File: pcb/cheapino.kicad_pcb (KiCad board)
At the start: 2 copper layers, 132.5 x 95.1 mm, 59 parts, among them K1 SW_Push, K10 SW_Push, K11 SW_Push, K12 SW_Push, K13 SW_Push, K14 SW_Push, K15 SW_Push, K16 SW_Push, K17 SW_Push, K18 SW_Push, K2 SW_Push, K3 SW_Push, K4 SW_Push, K5 SW_Push, K6 SW_Push, K7 SW_Push, K8 SW_Push, K9 SW_Push, U1 RP2040-Zero

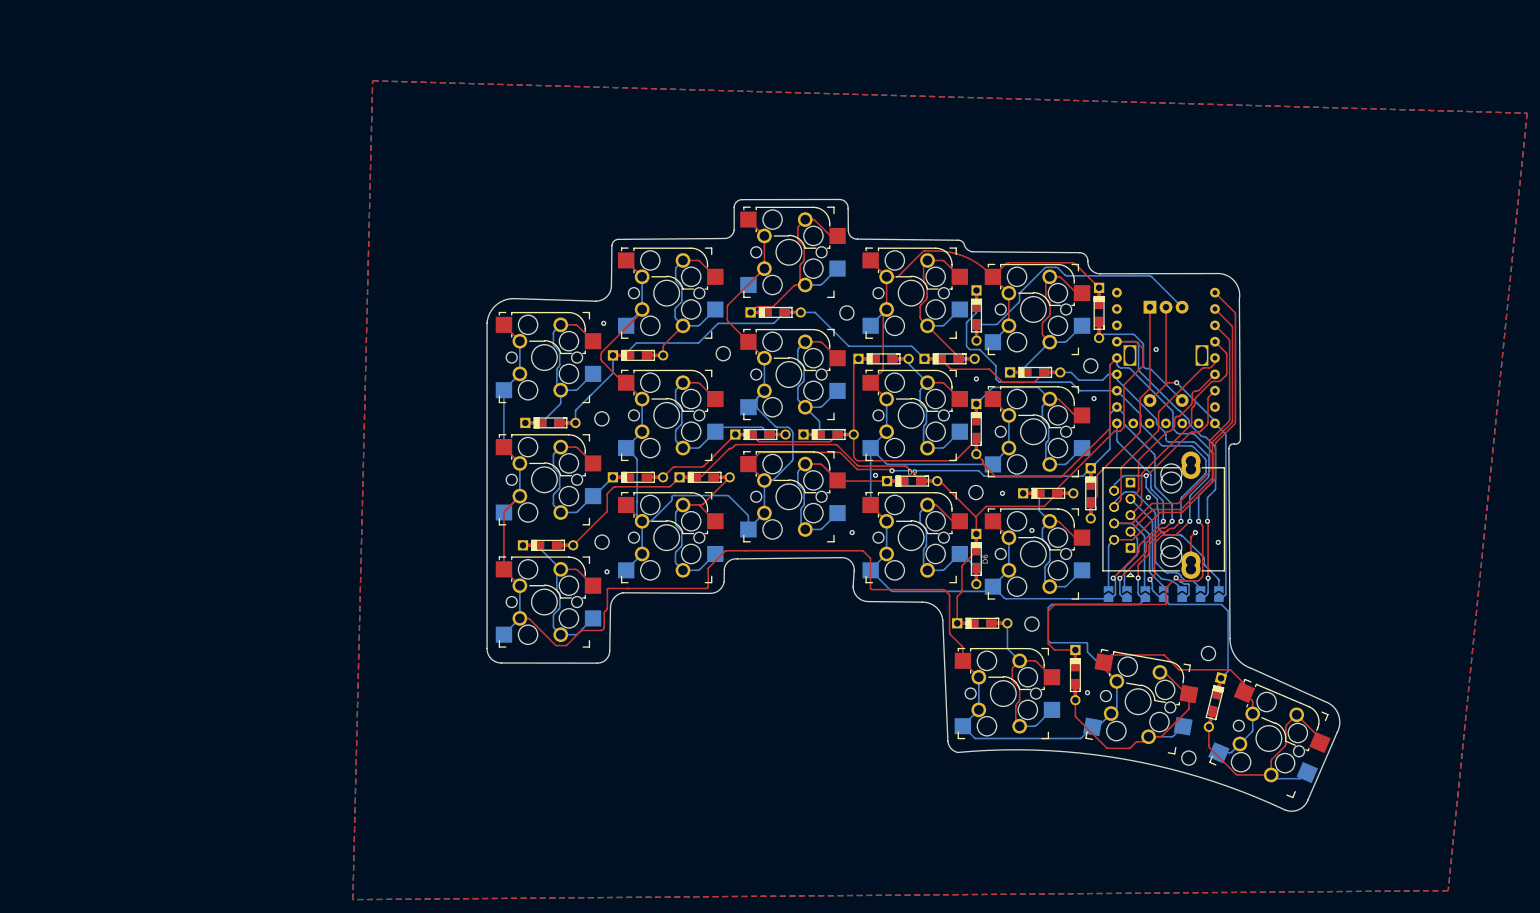
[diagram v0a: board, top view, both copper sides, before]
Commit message: Removed Rotary Encoder for space/flippability reasons and replaced all the key switch footprints that weren't bound properly to the schematic for some reason.
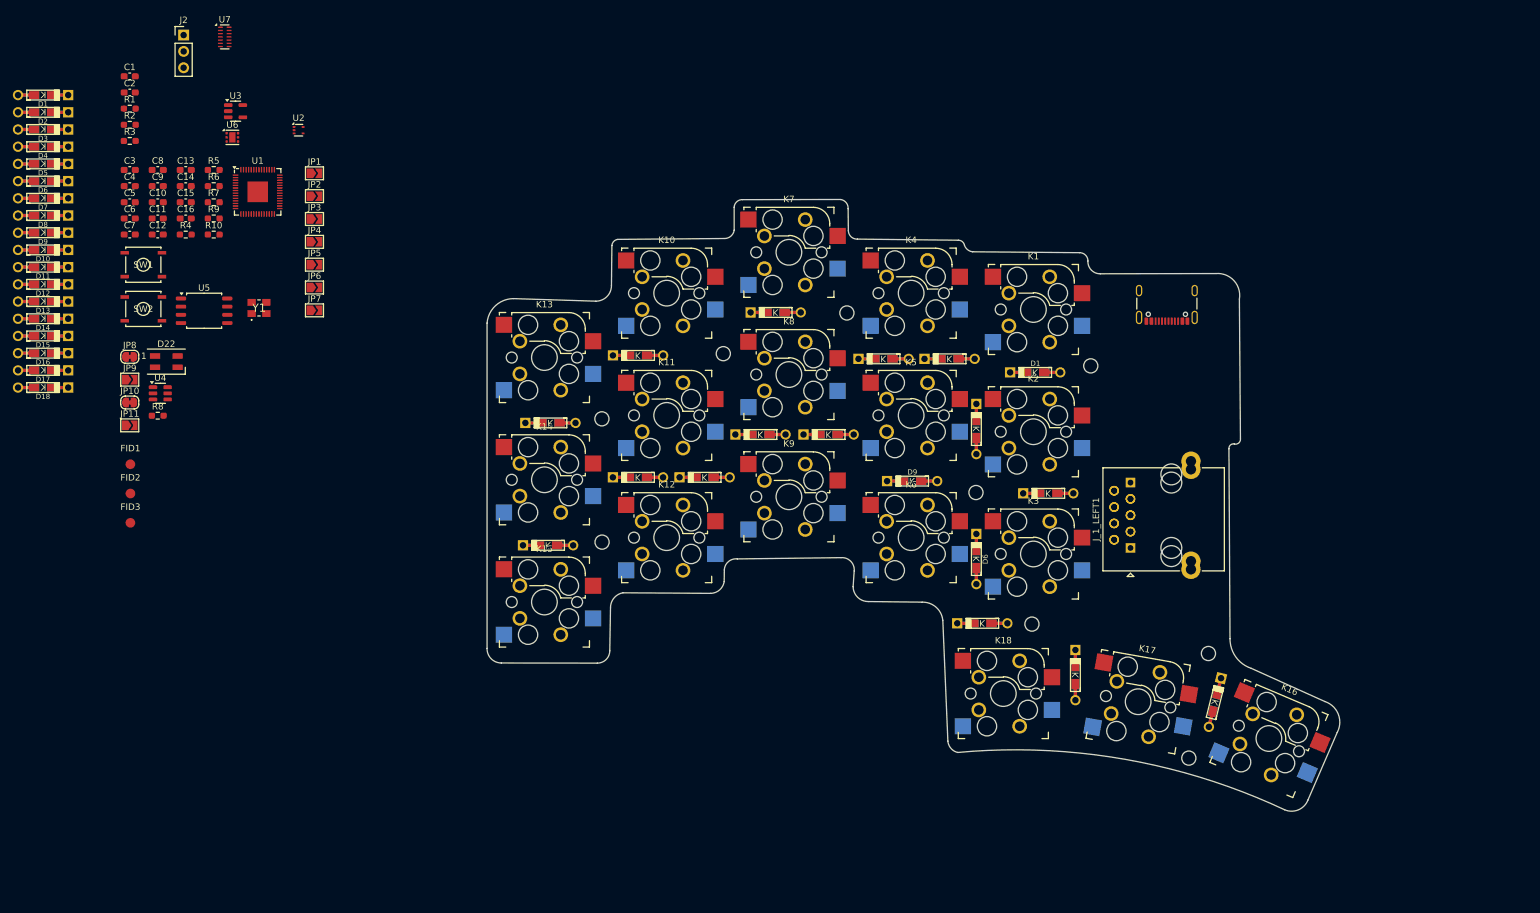
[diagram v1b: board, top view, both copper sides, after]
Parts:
- removed D19, D20, D21: DIODE, keebio:Diode-dual
- removed ENC1: RotaryEncoder_Switch, Rotary_Encoder:RotaryEncoder_Alps_EC11E-Switch_Vertical_H20mm
- added C1: 1μF, Capacitor_SMD:C_0603_1608Metric_Pad1.08x0.95mm_HandSolder, F.Cu at (4.57, 26.6)
- added C10: 1μF, Capacitor_SMD:C_0603_1608Metric_Pad1.08x0.95mm_HandSolder, F.Cu at (8.91, 46.2)
- added C11: 1μF, Capacitor_SMD:C_0603_1608Metric_Pad1.08x0.95mm_HandSolder, F.Cu at (8.91, 48.7)
- added C12: 100nF, Capacitor_SMD:C_0603_1608Metric_Pad1.08x0.95mm_HandSolder, F.Cu at (8.91, 51.2)
- added C13: 100nF, Capacitor_SMD:C_0603_1608Metric_Pad1.08x0.95mm_HandSolder, F.Cu at (13.3, 41.2)
- added C14: 15pF, Capacitor_SMD:C_0603_1608Metric_Pad1.08x0.95mm_HandSolder, F.Cu at (13.3, 43.7)
- added C15: 15pF, Capacitor_SMD:C_0603_1608Metric_Pad1.08x0.95mm_HandSolder, F.Cu at (13.3, 46.2)
- added C16: 100nF, Capacitor_SMD:C_0603_1608Metric_Pad1.08x0.95mm_HandSolder, F.Cu at (13.3, 48.7)
- added C2: 1μF, Capacitor_SMD:C_0603_1608Metric_Pad1.08x0.95mm_HandSolder, F.Cu at (4.57, 29.1)
- added C3: 100nF, Capacitor_SMD:C_0603_1608Metric_Pad1.08x0.95mm_HandSolder, F.Cu at (4.57, 41.2)
- added C4: 100nF, Capacitor_SMD:C_0603_1608Metric_Pad1.08x0.95mm_HandSolder, F.Cu at (4.57, 43.7)
- added C5: 100nF, Capacitor_SMD:C_0603_1608Metric_Pad1.08x0.95mm_HandSolder, F.Cu at (4.57, 46.2)
- added C6: 100nF, Capacitor_SMD:C_0603_1608Metric_Pad1.08x0.95mm_HandSolder, F.Cu at (4.57, 48.7)
- added C7: 100nF, Capacitor_SMD:C_0603_1608Metric_Pad1.08x0.95mm_HandSolder, F.Cu at (4.57, 51.2)
- added C8: 100nF, Capacitor_SMD:C_0603_1608Metric_Pad1.08x0.95mm_HandSolder, F.Cu at (8.91, 41.2)
- added C9: 100nF, Capacitor_SMD:C_0603_1608Metric_Pad1.08x0.95mm_HandSolder, F.Cu at (8.91, 43.7)
- added D1: DIODE, keebio:Diode-dual, F.Cu at (-8.90, 29.5)
- added D10: DIODE, keebio:Diode-dual, F.Cu at (-8.90, 53.6)
- added D11: DIODE, keebio:Diode-dual, F.Cu at (-8.90, 56.3)
- added D12: DIODE, keebio:Diode-dual, F.Cu at (-8.90, 59.0)
- added D13: DIODE, keebio:Diode-dual, F.Cu at (-8.90, 61.6)
- added D14: DIODE, keebio:Diode-dual, F.Cu at (-8.90, 64.3)
- added D15: DIODE, keebio:Diode-dual, F.Cu at (-8.90, 67.0)
- added D16: DIODE, keebio:Diode-dual, F.Cu at (-8.90, 69.7)
- added D17: DIODE, keebio:Diode-dual, F.Cu at (-8.90, 72.3)
- added D18: DIODE, keebio:Diode-dual, F.Cu at (-8.90, 75.0)
- added D2: DIODE, keebio:Diode-dual, F.Cu at (-8.90, 32.2)
- added D22: SK6812MINI, LED_SMD:LED_SK6812MINI_PLCC4_3.5x3.5mm_P1.75mm, F.Cu at (10.2, 71.0)
- added D3: DIODE, keebio:Diode-dual, F.Cu at (-8.90, 34.9)
- added D4: DIODE, keebio:Diode-dual, F.Cu at (-8.90, 37.6)
- added D5: DIODE, keebio:Diode-dual, F.Cu at (-8.90, 40.2)
- added D6: DIODE, keebio:Diode-dual, F.Cu at (-8.90, 42.9)
- added D7: DIODE, keebio:Diode-dual, F.Cu at (-8.90, 45.6)
- added D8: DIODE, keebio:Diode-dual, F.Cu at (-8.90, 48.3)
- added D9: DIODE, keebio:Diode-dual, F.Cu at (-8.90, 50.9)
- added FID1: Fiducial, Fiducial:Fiducial_1.5mm_Mask3mm, F.Cu at (4.67, 86.9)
- added FID2: Fiducial, Fiducial:Fiducial_1.5mm_Mask3mm, F.Cu at (4.67, 91.5)
- added FID3: Fiducial, Fiducial:Fiducial_1.5mm_Mask3mm, F.Cu at (4.67, 96.0)
- added J1: USB_C_Receptacle_USB2.0_16P, Connector_USB:USB_C_Receptacle_GCT_USB4105-xx-A_16P_TopMnt_Horizontal, F.Cu at (165.8, 61.0)
- added J2: DBG, Connector_PinHeader_2.54mm:PinHeader_1x03_P2.54mm_Vertical, F.Cu at (12.9, 20.2)
- added JP10: LED_DriveAs3V3, Jumper:SolderJumper-2_P1.3mm_Bridged_RoundedPad1.0x1.5mm, F.Cu at (4.57, 77.3)
- added JP11: LED_DriveAs5V, Jumper:SolderJumper-2_P1.3mm_Open_TrianglePad1.0x1.5mm, F.Cu at (4.57, 80.9)
- added JP8: LED_DriveAs3V3, Jumper:SolderJumper-2_P1.3mm_Bridged_RoundedPad1.0x1.5mm, F.Cu at (4.57, 70.2)
- added JP9: LED_DriveAs5V, Jumper:SolderJumper-2_P1.3mm_Open_TrianglePad1.0x1.5mm, F.Cu at (4.57, 73.8)
- added R1: 5.1k, Resistor_SMD:R_0603_1608Metric_Pad0.98x0.95mm_HandSolder, F.Cu at (4.57, 31.6)
- added R10: 1k, Resistor_SMD:R_0603_1608Metric_Pad0.98x0.95mm_HandSolder, F.Cu at (17.6, 51.2)
- added R2: 5.1k, Resistor_SMD:R_0603_1608Metric_Pad0.98x0.95mm_HandSolder, F.Cu at (4.57, 34.2)
- added R3: 10k, Resistor_SMD:R_0603_1608Metric_Pad0.98x0.95mm_HandSolder, F.Cu at (4.57, 36.7)
- added R4: 10k, Resistor_SMD:R_0603_1608Metric_Pad0.98x0.95mm_HandSolder, F.Cu at (13.3, 51.2)
- added R5: 27, Resistor_SMD:R_0603_1608Metric_Pad0.98x0.95mm_HandSolder, F.Cu at (17.6, 41.2)
- added R6: 27, Resistor_SMD:R_0603_1608Metric_Pad0.98x0.95mm_HandSolder, F.Cu at (17.6, 43.7)
- added R7: 1k, Resistor_SMD:R_0603_1608Metric_Pad0.98x0.95mm_HandSolder, F.Cu at (17.6, 46.2)
- added R8: 470, Resistor_SMD:R_0603_1608Metric_Pad0.98x0.95mm_HandSolder, F.Cu at (8.91, 79.4)
- added R9: 10k, Resistor_SMD:R_0603_1608Metric_Pad0.98x0.95mm_HandSolder, F.Cu at (17.6, 48.7)
- added SW1: BOOT, Extra:TL3342_EWI, F.Cu at (6.67, 55.9)
- added SW2: RST, Extra:TL3342_EWI, F.Cu at (6.67, 62.8)
- added U2: TPD2E2U06, Package_TO_SOT_SMD:SOT-553, F.Cu at (30.8, 35.0)
- added U3: AP2112K-3.3, Package_TO_SOT_SMD:SOT-23-5, F.Cu at (21.0, 32.0)
- added U4: TXS0101DBV, Package_TO_SOT_SMD:SOT-23-6, F.Cu at (9.31, 75.9)
- added U5: W25Q128JVSIQ, Package_SO:SOIC-8_5.23x5.23mm_P1.27mm, F.Cu at (16.1, 63.1)
- added U6: TVS0500DRV, Package_SON:WSON-6-1EP_2x2mm_P0.65mm_EP1x1.6mm, F.Cu at (20.5, 36.1)
- added U7: TPD6E05U06RVZ, Package_SON:Texas_R-PUSON-N14, F.Cu at (19.3, 20.5)
- added Y1: 12MHz, Extra:ABM8272T3, F.Cu at (24.6, 62.6)
- JP1, JP2, JP3, JP4, JP5, JP6, JP7: moved to F.Cu
- K1, K10, K11, K12, K13, K14, K15, K16, K17, K18, K2, K3, K4, K5, K6, K7, K8, K9: footprint project_footprints:Kailh_socket_MX_optional_reversible -> keyswitches:Kailh_socket_MX_optional_reversible
- U1: value RP2040-Zero -> RP2040; footprint rp2040:MCU_RP2040_Zero_34 -> Package_DFN_QFN:QFN-56-1EP_7x7mm_P0.4mm_EP3.2x3.2mm
- moved JP7 147.3 mm to (33.3, 63.0), turned to 0 degrees
- moved JP6 145.7 mm to (33.3, 59.5), turned to 0 degrees
- moved JP5 144.2 mm to (33.3, 55.9), turned to 0 degrees
- moved JP4 142.9 mm to (33.3, 52.4), turned to 0 degrees
- moved JP3 141.7 mm to (33.3, 48.8), turned to 0 degrees
- moved JP2 140.6 mm to (33.3, 45.2), turned to 0 degrees
- moved U1 140.6 mm to (24.4, 44.6)
- moved JP1 139.7 mm to (33.3, 41.7), turned to 0 degrees
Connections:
- JP1 pad 1: COL_1 -> /KeySwitches/COL_1
- JP1 pad 2: R_COL_1 -> /ExtConnectors/C_R_COL_1
- JP2 pad 1: COL_2 -> /KeySwitches/COL_2
- JP2 pad 2: R_COL_2 -> /ExtConnectors/C_R_COL_2
- JP3 pad 1: COL_3 -> /KeySwitches/COL_3
- JP3 pad 2: R_COL_3 -> /ExtConnectors/C_R_COL_3
- JP4 pad 1: ROW_1 -> /KeySwitches/ROW_1
- JP4 pad 2: R_ROW_1 -> /ExtConnectors/C_R_ROW_1
- JP5 pad 1: ROW_2 -> /KeySwitches/ROW_2
- JP5 pad 2: R_ROW_3 -> /ExtConnectors/C_R_ROW_3
- JP6 pad 1: ROW_3 -> /KeySwitches/ROW_3
- JP6 pad 2: R_ROW_2 -> /ExtConnectors/C_R_ROW_2
- JP7 pad 1: ROW_4 -> /LeftRightMapping/ROW_4
- JP7 pad 2: R_ROW_4 -> /LeftRightMapping/R_ROW_4
- J_1_LEFT1 pad 2: R_COL_1 -> /ExtConnectors/C_R_COL_1
- J_1_LEFT1 pad 3: R_COL_2 -> /ExtConnectors/C_R_COL_2
- J_1_LEFT1 pad 4: R_COL_3 -> /ExtConnectors/C_R_COL_3
- J_1_LEFT1 pad 5: R_ROW_1 -> /ExtConnectors/C_R_ROW_1
- J_1_LEFT1 pad 6: R_ROW_2 -> /ExtConnectors/C_R_ROW_2
- J_1_LEFT1 pad 7: R_ROW_3 -> /ExtConnectors/C_R_ROW_3
- J_1_LEFT1 pad 8: R_ROW_4 -> GND
- J_2_RIGHT1 pad 2: R_ROW_4 -> GND
- J_2_RIGHT1 pad 3: R_ROW_3 -> /ExtConnectors/C_R_ROW_3
- J_2_RIGHT1 pad 4: R_ROW_2 -> /ExtConnectors/C_R_ROW_2
- J_2_RIGHT1 pad 5: R_ROW_1 -> /ExtConnectors/C_R_ROW_1
- J_2_RIGHT1 pad 6: R_COL_3 -> /ExtConnectors/C_R_COL_3
- J_2_RIGHT1 pad 7: R_COL_2 -> /ExtConnectors/C_R_COL_2
- J_2_RIGHT1 pad 8: R_COL_1 -> /ExtConnectors/C_R_COL_1
- K1 pad 1: COL_1 -> /KeySwitches/COL_3
- K1 pad 2: Net-(D1-K) -> Net-(D1-A)
- K10 pad 1: COL_2 -> /KeySwitches/COL_2
- K10 pad 2: Net-(D10-A) -> Net-(D10-K)
- K11 pad 1: COL_2 -> /KeySwitches/COL_2
- K11 pad 2: Net-(D11-A) -> Net-(D11-K)
- K12 pad 1: COL_2 -> /KeySwitches/COL_2
- K12 pad 2: Net-(D12-A) -> Net-(D12-K)
- K13 pad 1: COL_3 -> /KeySwitches/COL_1
- K13 pad 2: Net-(D13-K) -> Net-(D13-A)
- K14 pad 1: COL_3 -> /KeySwitches/COL_1
- K14 pad 2: Net-(D14-K) -> Net-(D14-A)
- K15 pad 1: COL_3 -> /KeySwitches/COL_1
- K15 pad 2: Net-(D15-K) -> Net-(D15-A)
- K16 pad 1: COL_3 -> /KeySwitches/COL_1
- K16 pad 2: Net-(D16-A) -> Net-(D16-K)
- K17 pad 1: COL_3 -> /KeySwitches/COL_1
- K17 pad 2: Net-(D17-A) -> Net-(D17-K)
- K18 pad 1: COL_3 -> /KeySwitches/COL_1
- K18 pad 2: Net-(D18-A) -> Net-(D18-K)
- K2 pad 1: COL_1 -> /KeySwitches/COL_3
- K2 pad 2: Net-(D2-K) -> Net-(D2-A)
- K3 pad 1: COL_1 -> /KeySwitches/COL_3
- K3 pad 2: Net-(D3-K) -> Net-(D3-A)
- K4 pad 1: COL_1 -> /KeySwitches/COL_3
- K4 pad 2: Net-(D4-A) -> Net-(D4-K)
- K5 pad 1: COL_1 -> /KeySwitches/COL_3
- K5 pad 2: Net-(D5-A) -> Net-(D5-K)
- K6 pad 1: COL_1 -> /KeySwitches/COL_3
- K6 pad 2: Net-(D6-A) -> Net-(D6-K)
- K7 pad 1: COL_2 -> /KeySwitches/COL_2
- K7 pad 2: Net-(D7-K) -> Net-(D7-A)
- K8 pad 1: COL_2 -> /KeySwitches/COL_2
- K8 pad 2: Net-(D8-K) -> Net-(D8-A)
- K9 pad 1: COL_2 -> /KeySwitches/COL_2
- K9 pad 2: Net-(D9-K) -> Net-(D9-A)
- U1 pad 1: R_COL_2 -> +3V3
- U1 pad 10: unconnected-(U1-GP10-Pad10) -> +3V3
- U1 pad 11: unconnected-(U1-GP11-Pad11) -> /Microcontroller/ROW_4
- U1 pad 14: COL_1 -> unconnected-(U1-GPIO11-Pad14)
- U1 pad 15: COL_2 -> unconnected-(U1-GPIO12-Pad15)
- U1 pad 2: R_COL_3 -> /ExtConnectors/C_R_COL_1
- U1 pad 26: COL_3 -> Net-(U1-RUN)
- U1 pad 27: ROW_1 -> /Lighting/DIN_0
- U1 pad 28: ROW_2 -> unconnected-(U1-GPIO17-Pad28)
- U1 pad 29: ROW_3 -> unconnected-(U1-GPIO18-Pad29)
- U1 pad 3: R_ROW_1 -> /ExtConnectors/C_R_COL_2
- U1 pad 31: GND -> unconnected-(U1-GPIO20-Pad31)
- U1 pad 4: R_ROW_2 -> /ExtConnectors/C_R_COL_3
- U1 pad 5: R_ROW_3 -> /ExtConnectors/C_R_ROW_1
- U1 pad 6: R_ROW_4 -> /ExtConnectors/C_R_ROW_2
- U1 pad 7: unconnected-(U1-GP7-Pad7) -> /ExtConnectors/C_R_ROW_3
- U1 pad 8: ROW_4 -> /LeftRightMapping/R_ROW_4
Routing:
- net COL_3: track 355.4 -> 0.00 mm, vias 2 -> 0
- net COL_2: track 261.6 -> 0.00 mm, vias 3 -> 0
- net COL_1: track 229.2 -> 0.00 mm, vias 2 -> 0
- net ROW_2: track 187.7 -> 0.00 mm, vias 2 -> 0
- net ROW_3: track 181.0 -> 0.00 mm, vias 2 -> 0
- net ROW_1: track 160.5 -> 0.00 mm, vias 2 -> 0
- net R_COL_1: track 59.1 -> 0.00 mm
- net R_COL_3: track 56.9 -> 0.00 mm
- net R_ROW_2: track 55.6 -> 0.00 mm
- net R_COL_2: track 55.1 -> 0.00 mm
- net ROW_4: track 53.9 -> 0.00 mm, vias 1 -> 0
- net R_ROW_4: track 48.5 -> 0.00 mm, vias 1 -> 0
- net R_ROW_1: track 48.0 -> 0.00 mm
- net R_ROW_3: track 43.5 -> 0.00 mm
- net Net-(D20-A): track 38.8 -> 0.00 mm
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- removed copper zone on B.Cu, net GND
- removed copper zone on F.Cu, net GND

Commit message: Starting to position components and flipping passives as needed. Looking like board size is likely to need to be expanded.
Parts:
- removed the D1 at (-8.90, 29.5)
- removed the D10 at (-8.90, 53.6)
- removed the D11 at (-8.90, 56.3)
- removed the D12 at (-8.90, 59.0)
- removed the D13 at (-8.90, 61.6)
- removed the D14 at (-8.90, 64.3)
- removed the D15 at (-8.90, 67.0)
- removed the D16 at (-8.90, 69.7)
- removed the D17 at (-8.90, 72.3)
- removed the D18 at (-8.90, 75.0)
- removed the D2 at (-8.90, 32.2)
- removed the D3 at (-8.90, 34.9)
- removed the D4 at (-8.90, 37.6)
- removed the D5 at (-8.90, 40.2)
- removed the D6 at (-8.90, 42.9)
- removed the D7 at (-8.90, 45.6)
- removed the D8 at (-8.90, 48.3)
- removed the D9 at (-8.90, 50.9)
- FID1, FID2, FID3: footprint Fiducial:Fiducial_1.5mm_Mask3mm -> Fiducial:Fiducial_1mm_Mask2mm
- JP1, JP2, JP3, JP4, JP5, JP6, JP7: moved to B.Cu
- moved J2 204.7 mm to (217.2, 33.5)
- moved C10 201.2 mm to (210.1, 49.7)
- moved C11 201.2 mm to (210.1, 52.2)
- moved C12 201.2 mm to (210.1, 54.7)
- moved C8 201.2 mm to (210.1, 44.7)
- moved C9 201.2 mm to (210.1, 47.2)
- moved U1 201.2 mm to (225.6, 48.1)
- moved C13 201.2 mm to (214.5, 44.7)
- moved C14 201.2 mm to (214.5, 47.2)
- moved C15 201.2 mm to (214.5, 49.7)
- moved C16 201.2 mm to (214.5, 52.2)
- moved C3 201.2 mm to (205.8, 44.7)
- moved C4 201.2 mm to (205.8, 47.2)
- moved C5 201.2 mm to (205.8, 49.7)
- moved C6 201.2 mm to (205.8, 52.2)
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- renumbered D22 to D19
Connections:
- D1 pad 1: Net-(D1-K) -> /KeySwitches/ROW_1
- D1 pad 2: ROW_1 -> Net-(D1-A)
- D10 pad 1: ROW_1 -> Net-(D10-K)
- D10 pad 2: Net-(D10-A) -> /KeySwitches/ROW_1
- D11 pad 1: ROW_2 -> Net-(D11-K)
- D11 pad 2: Net-(D11-A) -> /KeySwitches/ROW_2
- D12 pad 1: ROW_3 -> Net-(D12-K)
- D12 pad 2: Net-(D12-A) -> /KeySwitches/ROW_3
- D13 pad 1: Net-(D13-K) -> /KeySwitches/ROW_1
- D13 pad 2: ROW_1 -> Net-(D13-A)
- D14 pad 1: Net-(D14-K) -> /KeySwitches/ROW_2
- D14 pad 2: ROW_2 -> Net-(D14-A)
- D15 pad 1: Net-(D15-K) -> /KeySwitches/ROW_3
- D15 pad 2: ROW_3 -> Net-(D15-A)
- D16 pad 1: ROW_1 -> Net-(D16-K)
- D16 pad 2: Net-(D16-A) -> /KeySwitches/ROW_1
- D17 pad 1: ROW_2 -> Net-(D17-K)
- D17 pad 2: Net-(D17-A) -> /KeySwitches/ROW_2
- D18 pad 1: ROW_3 -> Net-(D18-K)
- D18 pad 2: Net-(D18-A) -> /KeySwitches/ROW_3
- D2 pad 1: Net-(D2-K) -> /KeySwitches/ROW_2
- D2 pad 2: ROW_2 -> Net-(D2-A)
- D3 pad 1: Net-(D3-K) -> /KeySwitches/ROW_3
- D3 pad 2: ROW_3 -> Net-(D3-A)
- D4 pad 1: ROW_1 -> Net-(D4-K)
- D4 pad 2: Net-(D4-A) -> /KeySwitches/ROW_1
- D5 pad 1: ROW_2 -> Net-(D5-K)
- D5 pad 2: Net-(D5-A) -> /KeySwitches/ROW_2
- D6 pad 1: ROW_3 -> Net-(D6-K)
- D6 pad 2: Net-(D6-A) -> /KeySwitches/ROW_3
- D7 pad 1: Net-(D7-K) -> /KeySwitches/ROW_1
- D7 pad 2: ROW_1 -> Net-(D7-A)
- D8 pad 1: Net-(D8-K) -> /KeySwitches/ROW_2
- D8 pad 2: ROW_2 -> Net-(D8-A)
- D9 pad 1: Net-(D9-K) -> /KeySwitches/ROW_3
- D9 pad 2: ROW_3 -> Net-(D9-A)
- R2 pad 1: /ExtConnectors/CC2 -> GND
- R2 pad 2: GND -> /ExtConnectors/CC2
- R3 pad 1: VBUS -> Net-(U3-EN)
- R3 pad 2: Net-(U3-EN) -> VBUS

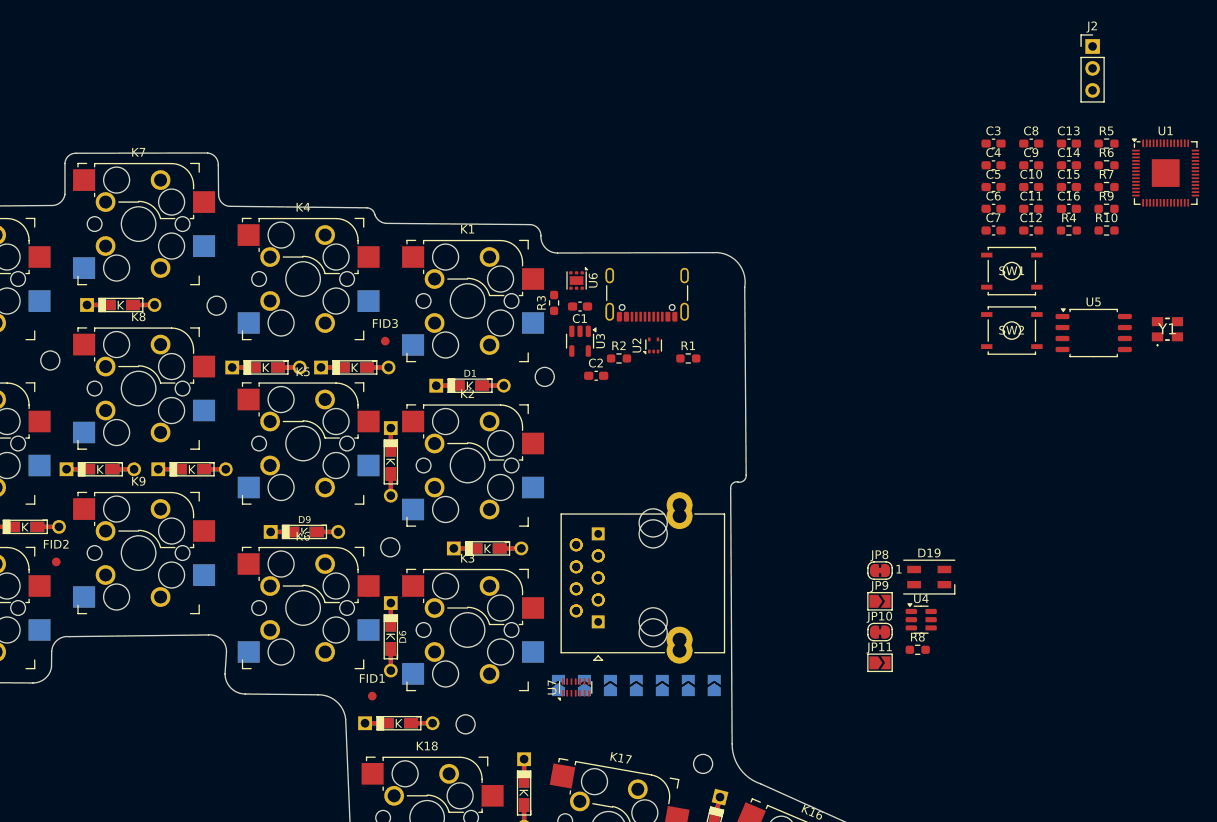
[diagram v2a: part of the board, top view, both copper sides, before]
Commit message: Placing more components onto the PCB and removing more stale leftovers from the now absent Rotary Encoder.
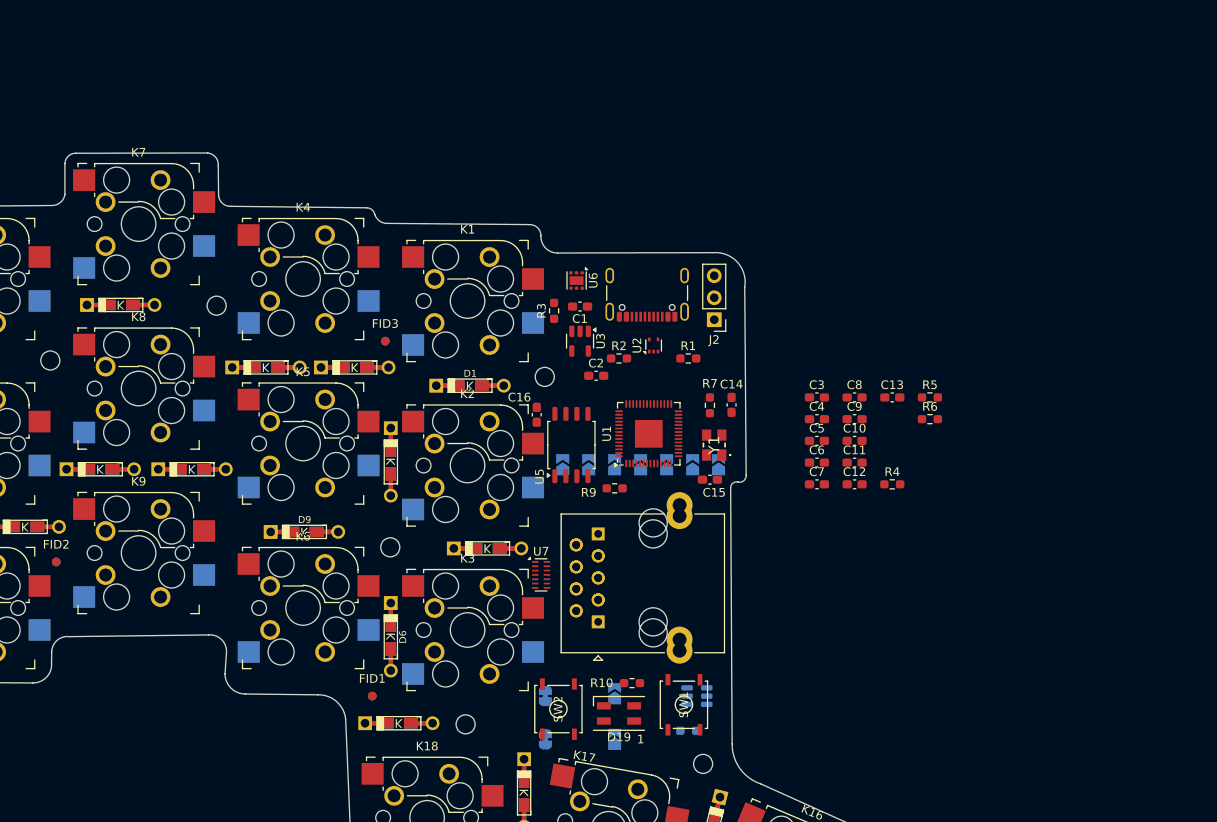
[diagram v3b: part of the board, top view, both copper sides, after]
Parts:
- added FID4: Fiducial, Fiducial:Fiducial_1mm_Mask2mm, B.Cu at (134.0, 108.5)
- added FID5: Fiducial, Fiducial:Fiducial_1mm_Mask2mm, B.Cu at (97.5, 93.0)
- added FID6: Fiducial, Fiducial:Fiducial_1mm_Mask2mm, B.Cu at (135.5, 67.5)
- JP10, JP11, JP8, JP9, R8, U4: moved to B.Cu
- moved R10 75.7 mm to (164.0, 107.0), turned to 180 degrees
- moved SW2 68.2 mm to (155.5, 110.0), turned to 90 degrees
- moved U1 66.9 mm to (165.9, 78.2), turned to 90 degrees
- moved C16 65.9 mm to (153.0, 76.0), turned to 90 degrees
- moved R9 65.3 mm to (162.0, 84.5), turned to 180 degrees
- moved SW1 62.8 mm to (170.0, 109.5), turned to 90 degrees
- moved U5 61.7 mm to (157.0, 79.5), turned to 90 degrees
- moved Y1 54.0 mm to (173.5, 79.5), turned to 90 degrees
- moved J2 53.9 mm to (173.5, 65.0), turned to 180 degrees
- moved C15 53.5 mm to (173.0, 83.5)
- moved R7 52.3 mm to (173.0, 74.9), turned to -90 degrees
- moved C14 47.8 mm to (175.5, 74.9), turned to -90 degrees
- moved JP8 41.3 mm to (154.0, 108.5), turned to 90 degrees
- moved JP10 40.6 mm to (154.0, 113.5), turned to 90 degrees
- moved D19 39.1 mm to (162.5, 110.5), turned to 180 degrees
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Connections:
- U1 pad 11: /Microcontroller/ROW_4 -> unconnected-(U1-GPIO8-Pad11)
- U1 pad 8: /LeftRightMapping/R_ROW_4 -> unconnected-(U1-GPIO6-Pad8)
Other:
- board text removed: "Cheapino 2"
- board text removed: "by Tompi"
